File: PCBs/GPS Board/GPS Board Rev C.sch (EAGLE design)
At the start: 4 parts

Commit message: Replace components with 0805s
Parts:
- C1, C2: device resistor:C-USC0603 -> resistor:C-USC0805
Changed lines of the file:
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@@
 <grid distance="0.1" unitdist="inch" unit="inch" style="lines" multiple="1" display="no" altdistance="0.01" altunitdist="inch" altunit="inch"/>
 <layers>
-<layer number="1" name="Top" color="4" fill="1" visible="no" active="no"/>
-<layer number="2" name="Route2" color="1" fill="3" visible="no" active="no"/>
-<layer number="3" name="Route3" color="4" fill="3" visible="no" active="no"/>
-<layer number="4" name="Route4" color="1" fill="4" visible="no" active="no"/>
-<layer number="5" name="Route5" color="4" fill="4" visible="no" active="no"/>
-<layer number="6" name="Route6" color="1" fill="8" visible="no" active="no"/>
-<layer number="7" name="Route7" color="4" fill="8" visible="no" active="no"/>
-<layer number="8" name="Route8" color="1" fill="2" visible="no" active="no"/>
-<layer number="9" name="Route9" color="4" fill="2" visible="no" active="no"/>
-<layer number="10" name="Route10" color="1" fill="7" visible="no" active="no"/>
-<layer number="11" name="Route11" color="4" fill="7" visible="no" active="no"/>
-<layer number="12" name="Route12" color="1" fill="5" visible="no" active="no"/>
-<layer number="13" name="Route13" color="4" fill="5" visible="no" active="no"/>
-<layer number="14" name="Route14" color="1" fill="6" visible="no" active="no"/>
-<layer number="15" name="Route15" color="4" fill="6" visible="no" active="no"/>
-<layer number="16" name="Bottom" color="1" fill="1" visible="no" active="no"/>
-<layer number="17" name="Pads" color="2" fill="1" visible="no" active="no"/>
-<layer number="18" name="Vias" color="2" fill="1" visible="no" active="no"/>
-<layer number="19" name="Unrouted" color="6" fill="1" visible="no" active="no"/>
-<layer number="20" name="Dimension" color="15" fill="1" visible="no" active="no"/>
-<layer number="21" name="tPlace" color="7" fill="1" visible="no" active="no"/>
-<layer number="22" name="bPlace" color="7" fill="1" visible="no" active="no"/>
-<layer number="23" name="tOrigins" color="15" fill="1" visible="no" active="no"/>
-<layer number="24" name="bOrigins" color="15" fill="1" visible="no" active="no"/>
-<layer number="25" name="tNames" color="7" fill="1" visible="no" active="no"/>
-<layer number="26" name="bNames" color="7" fill="1" visible="no" active="no"/>
-<layer number="27" name="tValues" color="7" fill="1" visible="no" active="no"/>
-<layer number="28" name="bValues" color="7" fill="1" visible="no" active="no"/>
+<layer number="1" name="Top" color="4" fill="1" visible="yes" active="no"/>
+<layer number="2" name="Route2" color="1" fill="3" visible="yes" active="no"/>
+<layer number="3" name="Route3" color="4" fill="3" visible="yes" active="no"/>
+<layer number="4" name="Route4" color="1" fill="4" visible="yes" active="no"/>
+<layer number="5" name="Route5" color="4" fill="4" visible="yes" active="no"/>
+<layer number="6" name="Route6" color="1" fill="8" visible="yes" active="no"/>
+<layer number="7" name="Route7" color="4" fill="8" visible="yes" active="no"/>
+<layer number="8" name="Route8" color="1" fill="2" visible="yes" active="no"/>
+<layer number="9" name="Route9" color="4" fill="2" visible="yes" active="no"/>
+<layer number="10" name="Route10" color="1" fill="7" visible="yes" active="no"/>
+<layer number="11" name="Route11" color="4" fill="7" visible="yes" active="no"/>
+<layer number="12" name="Route12" color="1" fill="5" visible="yes" active="no"/>
+<layer number="13" name="Route13" color="4" fill="5" visible="yes" active="no"/>
+<layer number="14" name="Route14" color="1" fill="6" visible="yes" active="no"/>
+<layer number="15" name="Route15" color="4" fill="6" visible="yes" active="no"/>
+<layer number="16" name="Bottom" color="1" fill="1" visible="yes" active="no"/>
+<layer number="17" name="Pads" color="2" fill="1" visible="yes" active="no"/>
+<layer number="18" name="Vias" color="2" fill="1" visible="yes" active="no"/>
+<layer number="19" name="Unrouted" color="6" fill="1" visible="yes" active="no"/>
+<layer number="20" name="Dimension" color="24" fill="1" visible="yes" active="no"/>
+<layer number="21" name="tPlace" color="7" fill="1" visible="yes" active="no"/>
+<layer number="22" name="bPlace" color="7" fill="1" visible="yes" active="no"/>
+<layer number="23" name="tOrigins" color="15" fill="1" visible="yes" active="no"/>
+<layer number="24" name="bOrigins" color="15" fill="1" visible="yes" active="no"/>
+<layer number="25" name="tNames" color="7" fill="1" visible="yes" active="no"/>
+<layer number="26" name="bNames" color="7" fill="1" visible="yes" active="no"/>
+<layer number="27" name="tValues" color="7" fill="1" visible="yes" active="no"/>
+<layer number="28" name="bValues" color="7" fill="1" visible="yes" active="no"/>
 <layer number="29" name="tStop" color="7" fill="3" visible="no" active="no"/>
 <layer number="30" name="bStop" color="7" fill="6" visible="no" active="no"/>
@@
 <layer number="35" name="tGlue" color="7" fill="4" visible="no" active="no"/>
 <layer number="36" name="bGlue" color="7" fill="5" visible="no" active="no"/>
-<layer number="37" name="tTest" color="7" fill="1" visible="no" active="no"/>
-<layer number="38" name="bTest" color="7" fill="1" visible="no" active="no"/>
+<layer number="37" name="tTest" color="7" fill="1" visible="yes" active="no"/>
+<layer number="38" name="bTest" color="7" fill="1" visible="yes" active="no"/>
 <layer number="39" name="tKeepout" color="4" fill="11" visible="no" active="no"/>
 <layer number="40" name="bKeepout" color="1" fill="11" visible="no" active="no"/>
@@
 <layer number="44" name="Drills" color="7" fill="1" visible="no" active="no"/>
 <layer number="45" name="Holes" color="7" fill="1" visible="no" active="no"/>
-<layer number="46" name="Milling" color="3" fill="1" visible="no" active="no"/>
-<layer number="47" name="Measures" color="7" fill="1" visible="no" active="no"/>
-<layer number="48" name="Document" color="7" fill="1" visible="no" active="no"/>
-<layer number="49" name="Reference" color="7" fill="1" visible="no" active="no"/>
-<layer number="50" name="dxf" color="7" fill="1" visible="no" active="no"/>
-<layer number="51" name="tDocu" color="7" fill="1" visible="no" active="no"/>
-<layer number="52" name="bDocu" color="7" fill="1" visible="no" active="no"/>
-<layer number="53" name="tGND_GNDA" color="7" fill="9" visible="no" active="no"/>
-<layer number="54" name="bGND_GNDA" color="1" fill="9" visible="no" active="no"/>
-<layer number="56" name="wert" color="7" fill="1" visible="no" active="no"/>
-<layer number="57" name="tCAD" color="7" fill="1" visible="no" active="no"/>
+<layer number="46" name="Milling" color="3" fill="1" visible="yes" active="no"/>
+<layer number="47" name="Measures" color="7" fill="1" visible="yes" active="no"/>
+<layer number="48" name="Document" color="7" fill="1" visible="yes" active="no"/>
+<layer number="49" name="Reference" color="7" fill="1" visible="yes" active="no"/>
+<layer number="50" name="dxf" color="7" fill="1" visible="yes" active="no"/>
+<layer number="51" name="tDocu" color="7" fill="1" visible="yes" active="no"/>
+<layer number="52" name="bDocu" color="7" fill="1" visible="yes" active="no"/>
+<layer number="53" name="tGND_GNDA" color="7" fill="9" visible="yes" active="no"/>
+<layer number="54" name="bGND_GNDA" color="1" fill="9" visible="yes" active="no"/>
+<layer number="56" name="wert" color="7" fill="1" visible="yes" active="no"/>
+<layer number="57" name="tCAD" color="7" fill="1" visible="yes" active="no"/>
 <layer number="88" name="SimResults" color="9" fill="1" visible="yes" active="yes"/>
 <layer number="89" name="SimProbes" color="9" fill="1" visible="yes" active="yes"/>
@@
 <part name="U$1" library="pinavl1" deviceset="PINAVL1" device=""/>
 <part name="U$2" library="Cubesat" deviceset="PC104" device=""/>
-<part name="C2" library="resistor" library_urn="urn:adsk.eagle:library:348" deviceset="C-US" device="C0603" package3d_urn="urn:adsk.eagle:package:26138/1" value="1uF"/>
-<part name="C1" library="resistor" library_urn="urn:adsk.eagle:library:348" deviceset="C-US" device="C0603" package3d_urn="urn:adsk.eagle:package:26138/1" value="0.1uF"/>
+<part name="C2" library="resistor" library_urn="urn:adsk.eagle:library:348" deviceset="C-US" device="C0805" package3d_urn="urn:adsk.eagle:package:26137/1" value="1uF"/>
+<part name="C1" library="resistor" library_urn="urn:adsk.eagle:library:348" deviceset="C-US" device="C0805" package3d_urn="urn:adsk.eagle:package:26137/1" value="0.1uF"/>
 </parts>
 <sheets>

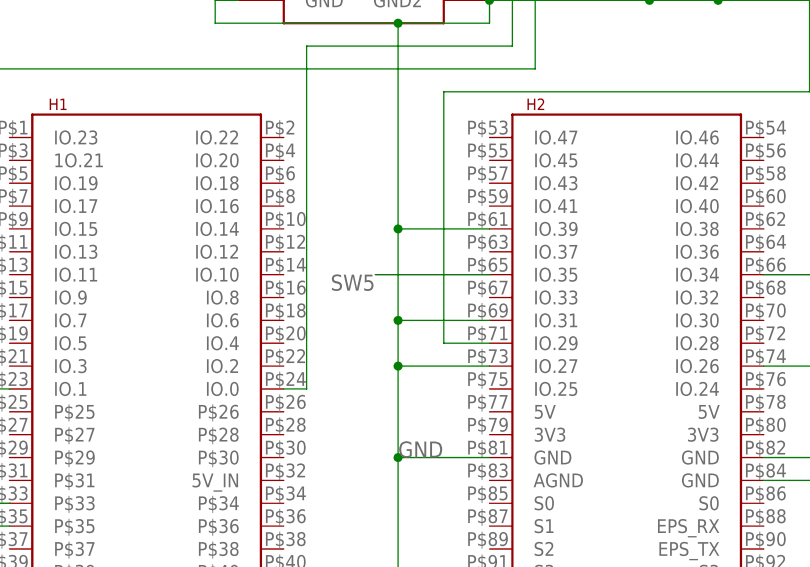
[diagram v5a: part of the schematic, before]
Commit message: Make GPS board pass ERC and DRC
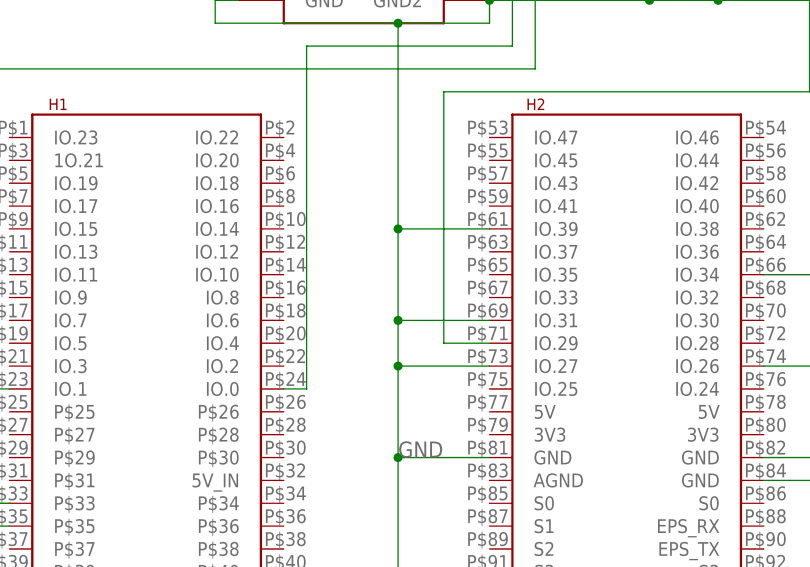
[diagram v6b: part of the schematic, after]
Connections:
- removed net SW5: U$2.IO.35
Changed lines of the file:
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@@
 <grid distance="0.1" unitdist="inch" unit="inch" style="lines" multiple="1" display="no" altdistance="0.01" altunitdist="inch" altunit="inch"/>
 <layers>
-<layer number="1" name="Top" color="4" fill="1" visible="yes" active="no"/>
-<layer number="2" name="Route2" color="1" fill="3" visible="yes" active="no"/>
-<layer number="3" name="Route3" color="4" fill="3" visible="yes" active="no"/>
-<layer number="4" name="Route4" color="1" fill="4" visible="yes" active="no"/>
-<layer number="5" name="Route5" color="4" fill="4" visible="yes" active="no"/>
-<layer number="6" name="Route6" color="1" fill="8" visible="yes" active="no"/>
-<layer number="7" name="Route7" color="4" fill="8" visible="yes" active="no"/>
-<layer number="8" name="Route8" color="1" fill="2" visible="yes" active="no"/>
-<layer number="9" name="Route9" color="4" fill="2" visible="yes" active="no"/>
-<layer number="10" name="Route10" color="1" fill="7" visible="yes" active="no"/>
-<layer number="11" name="Route11" color="4" fill="7" visible="yes" active="no"/>
-<layer number="12" name="Route12" color="1" fill="5" visible="yes" active="no"/>
-<layer number="13" name="Route13" color="4" fill="5" visible="yes" active="no"/>
-<layer number="14" name="Route14" color="1" fill="6" visible="yes" active="no"/>
-<layer number="15" name="Route15" color="4" fill="6" visible="yes" active="no"/>
-<layer number="16" name="Bottom" color="1" fill="1" visible="yes" active="no"/>
-<layer number="17" name="Pads" color="2" fill="1" visible="yes" active="no"/>
-<layer number="18" name="Vias" color="2" fill="1" visible="yes" active="no"/>
-<layer number="19" name="Unrouted" color="6" fill="1" visible="yes" active="no"/>
-<layer number="20" name="Dimension" color="24" fill="1" visible="yes" active="no"/>
-<layer number="21" name="tPlace" color="7" fill="1" visible="yes" active="no"/>
-<layer number="22" name="bPlace" color="7" fill="1" visible="yes" active="no"/>
-<layer number="23" name="tOrigins" color="15" fill="1" visible="yes" active="no"/>
-<layer number="24" name="bOrigins" color="15" fill="1" visible="yes" active="no"/>
-<layer number="25" name="tNames" color="7" fill="1" visible="yes" active="no"/>
-<layer number="26" name="bNames" color="7" fill="1" visible="yes" active="no"/>
-<layer number="27" name="tValues" color="7" fill="1" visible="yes" active="no"/>
-<layer number="28" name="bValues" color="7" fill="1" visible="yes" active="no"/>
+<layer number="1" name="Top" color="4" fill="1" visible="no" active="no"/>
+<layer number="2" name="Route2" color="1" fill="3" visible="no" active="no"/>
+<layer number="3" name="Route3" color="4" fill="3" visible="no" active="no"/>
+<layer number="4" name="Route4" color="1" fill="4" visible="no" active="no"/>
+<layer number="5" name="Route5" color="4" fill="4" visible="no" active="no"/>
+<layer number="6" name="Route6" color="1" fill="8" visible="no" active="no"/>
+<layer number="7" name="Route7" color="4" fill="8" visible="no" active="no"/>
+<layer number="8" name="Route8" color="1" fill="2" visible="no" active="no"/>
+<layer number="9" name="Route9" color="4" fill="2" visible="no" active="no"/>
+<layer number="10" name="Route10" color="1" fill="7" visible="no" active="no"/>
+<layer number="11" name="Route11" color="4" fill="7" visible="no" active="no"/>
+<layer number="12" name="Route12" color="1" fill="5" visible="no" active="no"/>
+<layer number="13" name="Route13" color="4" fill="5" visible="no" active="no"/>
+<layer number="14" name="Route14" color="1" fill="6" visible="no" active="no"/>
+<layer number="15" name="Route15" color="4" fill="6" visible="no" active="no"/>
+<layer number="16" name="Bottom" color="1" fill="1" visible="no" active="no"/>
+<layer number="17" name="Pads" color="2" fill="1" visible="no" active="no"/>
+<layer number="18" name="Vias" color="2" fill="1" visible="no" active="no"/>
+<layer number="19" name="Unrouted" color="6" fill="1" visible="no" active="no"/>
+<layer number="20" name="Dimension" color="24" fill="1" visible="no" active="no"/>
+<layer number="21" name="tPlace" color="7" fill="1" visible="no" active="no"/>
+<layer number="22" name="bPlace" color="7" fill="1" visible="no" active="no"/>
+<layer number="23" name="tOrigins" color="15" fill="1" visible="no" active="no"/>
+<layer number="24" name="bOrigins" color="15" fill="1" visible="no" active="no"/>
+<layer number="25" name="tNames" color="7" fill="1" visible="no" active="no"/>
+<layer number="26" name="bNames" color="7" fill="1" visible="no" active="no"/>
+<layer number="27" name="tValues" color="7" fill="1" visible="no" active="no"/>
+<layer number="28" name="bValues" color="7" fill="1" visible="no" active="no"/>
 <layer number="29" name="tStop" color="7" fill="3" visible="no" active="no"/>
 <layer number="30" name="bStop" color="7" fill="6" visible="no" active="no"/>
@@
 <layer number="35" name="tGlue" color="7" fill="4" visible="no" active="no"/>
 <layer number="36" name="bGlue" color="7" fill="5" visible="no" active="no"/>
-<layer number="37" name="tTest" color="7" fill="1" visible="yes" active="no"/>
-<layer number="38" name="bTest" color="7" fill="1" visible="yes" active="no"/>
+<layer number="37" name="tTest" color="7" fill="1" visible="no" active="no"/>
+<layer number="38" name="bTest" color="7" fill="1" visible="no" active="no"/>
 <layer number="39" name="tKeepout" color="4" fill="11" visible="no" active="no"/>
 <layer number="40" name="bKeepout" color="1" fill="11" visible="no" active="no"/>
@@
 <layer number="44" name="Drills" color="7" fill="1" visible="no" active="no"/>
 <layer number="45" name="Holes" color="7" fill="1" visible="no" active="no"/>
-<layer number="46" name="Milling" color="3" fill="1" visible="yes" active="no"/>
-<layer number="47" name="Measures" color="7" fill="1" visible="yes" active="no"/>
-<layer number="48" name="Document" color="7" fill="1" visible="yes" active="no"/>
-<layer number="49" name="Reference" color="7" fill="1" visible="yes" active="no"/>
-<layer number="50" name="dxf" color="7" fill="1" visible="yes" active="no"/>
-<layer number="51" name="tDocu" color="7" fill="1" visible="yes" active="no"/>
-<layer number="52" name="bDocu" color="7" fill="1" visible="yes" active="no"/>
-<layer number="53" name="tGND_GNDA" color="7" fill="9" visible="yes" active="no"/>
-<layer number="54" name="bGND_GNDA" color="1" fill="9" visible="yes" active="no"/>
-<layer number="56" name="wert" color="7" fill="1" visible="yes" active="no"/>
-<layer number="57" name="tCAD" color="7" fill="1" visible="yes" active="no"/>
+<layer number="46" name="Milling" color="3" fill="1" visible="no" active="no"/>
+<layer number="47" name="Measures" color="7" fill="1" visible="no" active="no"/>
+<layer number="48" name="Document" color="7" fill="1" visible="no" active="no"/>
+<layer number="49" name="Reference" color="7" fill="1" visible="no" active="no"/>
+<layer number="50" name="dxf" color="7" fill="1" visible="no" active="no"/>
+<layer number="51" name="tDocu" color="7" fill="1" visible="no" active="no"/>
+<layer number="52" name="bDocu" color="7" fill="1" visible="no" active="no"/>
+<layer number="53" name="tGND_GNDA" color="7" fill="9" visible="no" active="no"/>
+<layer number="54" name="bGND_GNDA" color="1" fill="9" visible="no" active="no"/>
+<layer number="56" name="wert" color="7" fill="1" visible="no" active="no"/>
+<layer number="57" name="tCAD" color="7" fill="1" visible="no" active="no"/>
 <layer number="88" name="SimResults" color="9" fill="1" visible="yes" active="yes"/>
 <layer number="89" name="SimProbes" color="9" fill="1" visible="yes" active="yes"/>
@@
 </segment>
 </net>
-<net name="SW5" class="0">
-<segment>
-<pinref part="U$2" gate="G$1" pin="IO.35"/>
-<wire x1="45.72" y1="43.18" x2="33.02" y2="43.18" width="0.1524" layer="91"/>
-<label x="33.02" y="43.18" size="1.778" layer="95" rot="R180"/>
-</segment>
-</net>
